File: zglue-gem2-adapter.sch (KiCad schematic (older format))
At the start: 77 parts, among them J1 543630489, J2 543630489, U1 zGlue-Jade

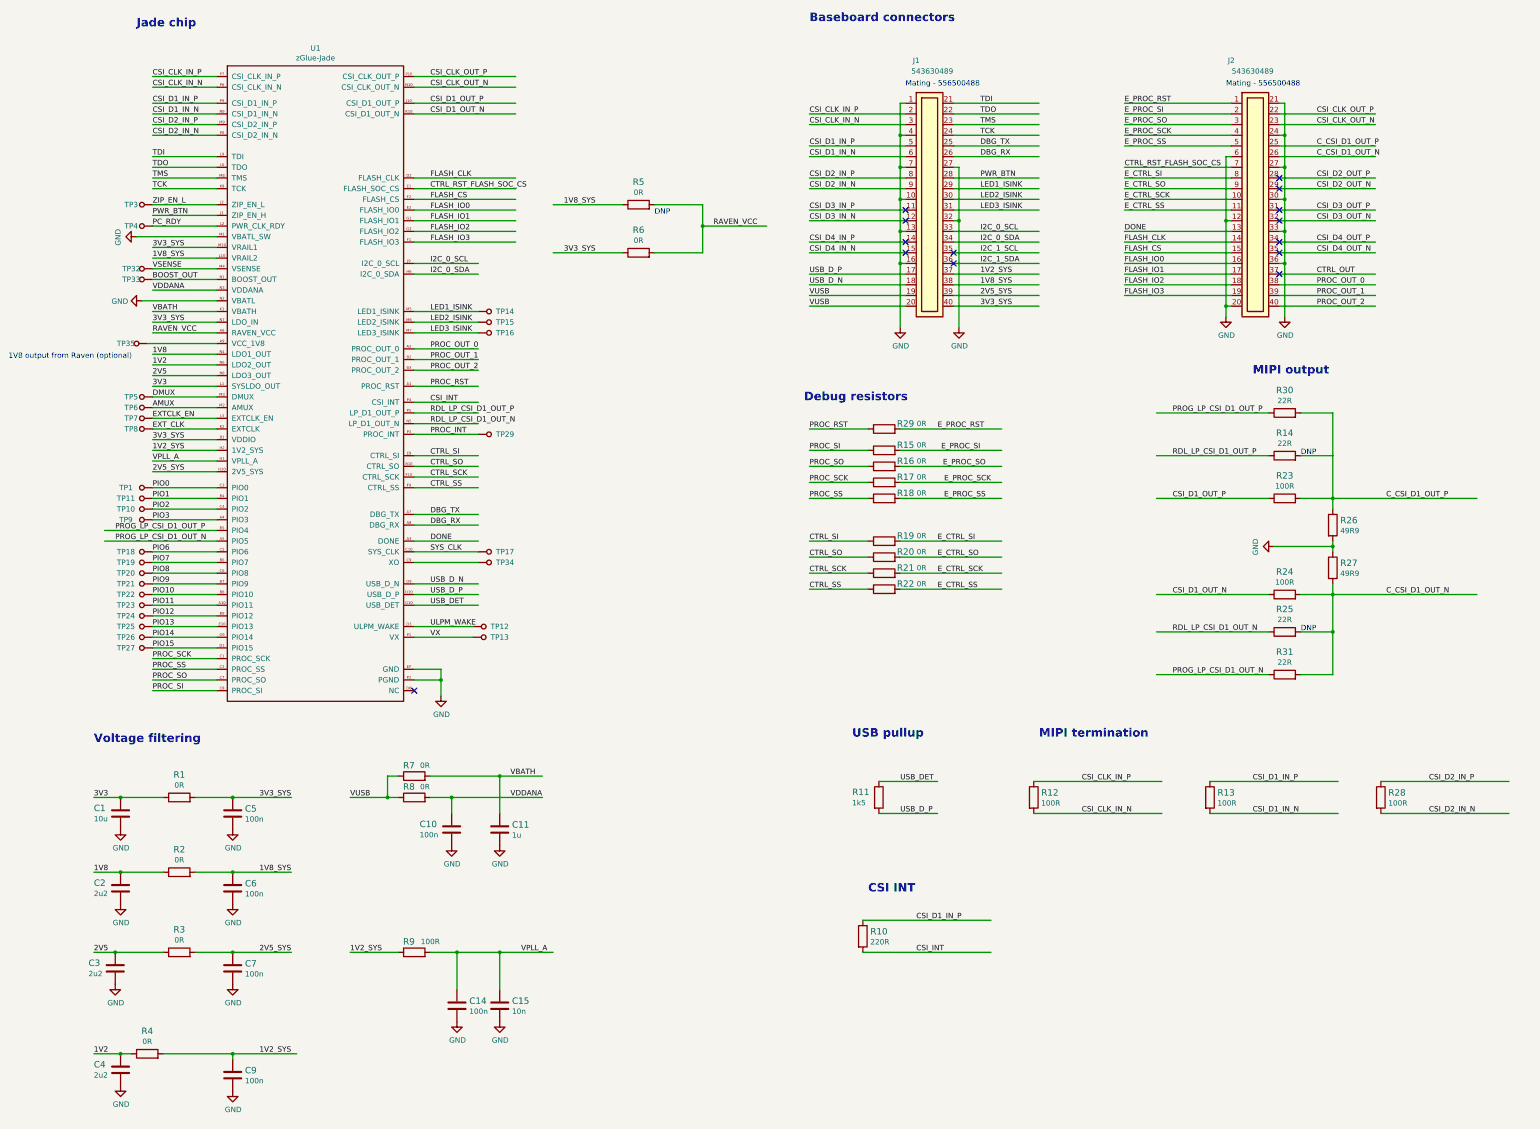
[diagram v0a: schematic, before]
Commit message: Update GEM2 symbol
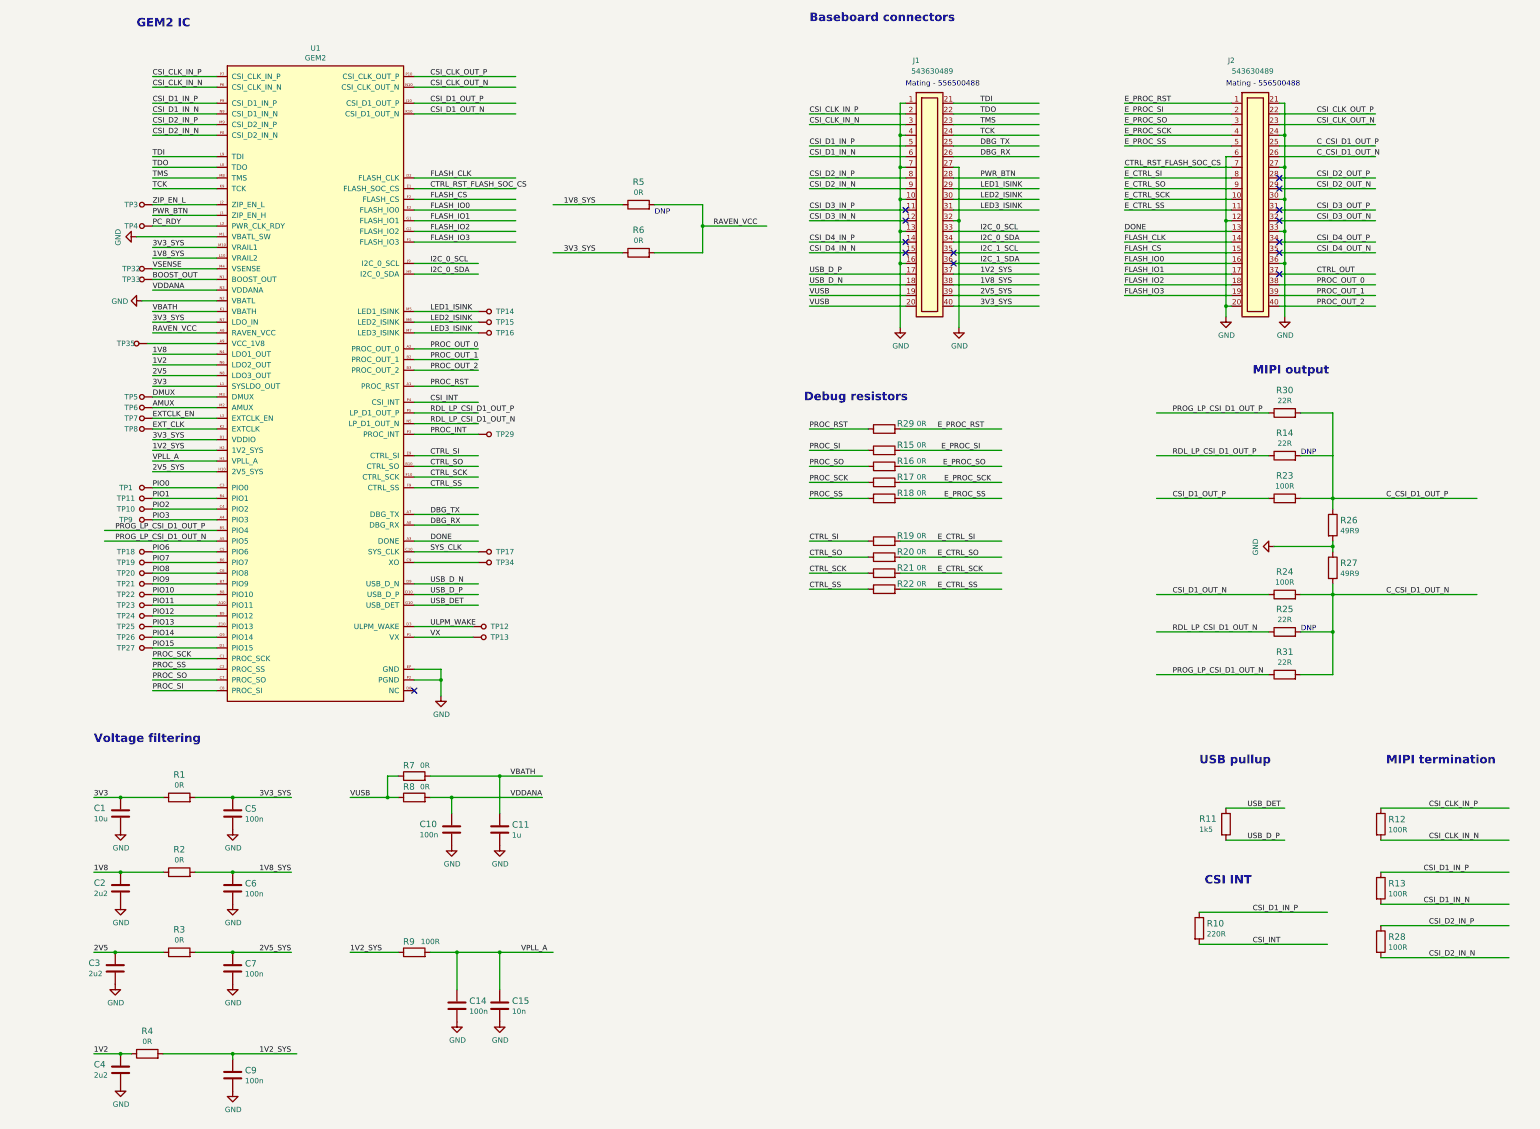
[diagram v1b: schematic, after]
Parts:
- removed U1: zGlue-Jade, zglue-jade-adapter-footprints:Z-Glue_LGA-96, symbol zglue-jade-adapter:zGlue-Jade-zglue-jade
- added U1: GEM2, zglue-jade-adapter-footprints:Z-Glue_LGA-96, symbol zglue-jade-adapter:GEM2
- R14, R25: DNP (none) -> 1
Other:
- note added: "GEM2 IC"
- note removed: "1V8 output from Raven (optional)"
- note removed: "Jade chip"
- moved on the sheet: R10, R11, R12, R13, R28
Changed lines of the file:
@@
 EESchema Schematic File Version 4
-LIBS:zglue-gem2-adapter-cache
 EELAYER 30 0
 EELAYER END
@@
 1V2
 Text Notes 1600 850  0    79   ~ 16
-Jade chip
+GEM2 IC
 $Comp
 L zglue-jade-adapter:C_100n_0402_6V3 C5
@@
 Text Label 10850 2750 0    50   ~ 0
 DONE
-Text Label 8750 7900 0    50   ~ 0
+Text Label 12000 8150 0    50   ~ 0
 USB_DET
 Text Label 7900 3250 0    50   ~ 0
@@
 L zglue-jade-adapter:R_1k5_0402 R11
 U 1 1 5DCE918C
-P 8550 8050
-F 0 "R11" V 8500 7800 60  0000 L CNN
-F 1 "R_1k5_0402" H 8550 7900 60  0001 C CNN
-F 2 "zglue-jade-adapter-footprints:0402-res" H 8750 8250 60  0001 L CNN
-F 3 "" H 8550 8050 50  0001 C CNN
-F 4 "PANASONIC_ELECTRONIC_COMPONENTS" H 8750 8450 60  0001 L CNN "Manufacturer"
-F 5 "ERJ2RKF1501X" H 8750 8350 60  0001 L CNN "MPN"
-F 6 "1k5" V 8600 7800 50  0000 L CNN "Val"
-	1    8550 8050
-	0    1    1    0
-$EndComp
-Text Label 8750 8200 0    50   ~ 0
+P 11800 8300
+F 0 "R11" V 11750 8050 60  0000 L CNN
+F 1 "R_1k5_0402" H 11800 8150 60  0001 C CNN
+F 2 "zglue-jade-adapter-footprints:0402-res" H 12000 8500 60  0001 L CNN
+F 3 "" H 11800 8300 50  0001 C CNN
+F 4 "PANASONIC_ELECTRONIC_COMPONENTS" H 12000 8700 60  0001 L CNN "Manufacturer"
+F 5 "ERJ2RKF1501X" H 12000 8600 60  0001 L CNN "MPN"
+F 6 "1k5" V 11850 8050 50  0000 L CNN "Val"
+	1    11800 8300
+	0    1    1    0
+$EndComp
+Text Label 12000 8450 0    50   ~ 0
 USB_D_P
 Wire Wire Line
-	8550 7900 9100 7900
-Wire Wire Line
-	8550 8200 9100 8200
+	11800 8150 12350 8150
+Wire Wire Line
+	11800 8450 12350 8450
 Text Notes 8800 1400 0    50   ~ 0
 Mating - 556500488
@@
 Wire Wire Line
 	8750 6100 9700 6100
-Text Notes 8300 7500 0    79   ~ 16
+Text Notes 11550 7750 0    79   ~ 16
 USB pullup
 Text Label 9500 2350 0    50   ~ 0
@@
 Wire Wire Line
 	2350 3800 1700 3800
-Text Notes 400  3950 0    50   ~ 0
-1V8 output from Raven (optional)
 Wire Wire Line
 	1850 10450 2500 10450
@@
 L zglue-jade-adapter:R_100R_0402 R12
 U 1 1 5DC3B849
-P 10000 8050
-F 0 "R12" V 9955 8120 60  0000 L CNN
-F 1 "R_100R_0402" H 10000 7900 60  0001 C CNN
-F 2 "zglue-jade-adapter-footprints:0402-res" H 10200 8250 60  0001 L CNN
-F 3 "" H 10000 8050 50  0001 C CNN
-F 4 "BOURNS" H 10200 8450 60  0001 L CNN "Manufacturer"
-F 5 "CR0402-FX-1000GLF" H 10200 8350 60  0001 L CNN "MPN"
-F 6 "100R" V 10053 8120 50  0000 L CNN "Val"
-	1    10000 8050
-	0    1    1    0
-$EndComp
-Wire Wire Line
-	10000 7900 11200 7900
-Wire Wire Line
-	10000 8200 11200 8200
-Text Label 10450 7900 0    50   ~ 0
+P 13250 8300
+F 0 "R12" V 13205 8370 60  0000 L CNN
+F 1 "R_100R_0402" H 13250 8150 60  0001 C CNN
+F 2 "zglue-jade-adapter-footprints:0402-res" H 13450 8500 60  0001 L CNN
+F 3 "" H 13250 8300 50  0001 C CNN
+F 4 "BOURNS" H 13450 8700 60  0001 L CNN "Manufacturer"
+F 5 "CR0402-FX-1000GLF" H 13450 8600 60  0001 L CNN "MPN"
+F 6 "100R" V 13303 8370 50  0000 L CNN "Val"
+	1    13250 8300
+	0    1    1    0
+$EndComp
+Wire Wire Line
+	13250 8150 14450 8150
+Wire Wire Line
+	13250 8450 14450 8450
+Text Label 13700 8150 0    50   ~ 0
 CSI_CLK_IN_P
-Text Label 10450 8200 0    50   ~ 0
+Text Label 13700 8450 0    50   ~ 0
 CSI_CLK_IN_N
 $Comp
 L zglue-jade-adapter:R_100R_0402 R13
 U 1 1 5DC8AA98
-P 11650 8050
-F 0 "R13" V 11605 8120 60  0000 L CNN
-F 1 "R_100R_0402" H 11650 7900 60  0001 C CNN
-F 2 "zglue-jade-adapter-footprints:0402-res" H 11850 8250 60  0001 L CNN
-F 3 "" H 11650 8050 50  0001 C CNN
-F 4 "BOURNS" H 11850 8450 60  0001 L CNN "Manufacturer"
-F 5 "CR0402-FX-1000GLF" H 11850 8350 60  0001 L CNN "MPN"
-F 6 "100R" V 11703 8120 50  0000 L CNN "Val"
-	1    11650 8050
-	0    1    1    0
-$EndComp
-Wire Wire Line
-	11650 7900 12850 7900
-Wire Wire Line
-	11650 8200 12850 8200
+P 13250 8900
+F 0 "R13" V 13205 8970 60  0000 L CNN
+F 1 "R_100R_0402" H 13250 8750 60  0001 C CNN
+F 2 "zglue-jade-adapter-footprints:0402-res" H 13450 9100 60  0001 L CNN
+F 3 "" H 13250 8900 50  0001 C CNN
+F 4 "BOURNS" H 13450 9300 60  0001 L CNN "Manufacturer"
+F 5 "CR0402-FX-1000GLF" H 13450 9200 60  0001 L CNN "MPN"
+F 6 "100R" V 13303 8970 50  0000 L CNN "Val"
+	1    13250 8900
+	0    1    1    0
+$EndComp
+Wire Wire Line
+	13250 8750 14450 8750
+Wire Wire Line
+	13250 9050 14450 9050
 $Comp
 L zglue-jade-adapter:R_100R_0402 R28
 U 1 1 5DCA538B
-P 13250 8050
-F 0 "R28" V 13205 8120 60  0000 L CNN
-F 1 "R_100R_0402" H 13250 7900 60  0001 C CNN
-F 2 "zglue-jade-adapter-footprints:0402-res" H 13450 8250 60  0001 L CNN
-F 3 "" H 13250 8050 50  0001 C CNN
-F 4 "BOURNS" H 13450 8450 60  0001 L CNN "Manufacturer"
-F 5 "CR0402-FX-1000GLF" H 13450 8350 60  0001 L CNN "MPN"
-F 6 "100R" V 13303 8120 50  0000 L CNN "Val"
-	1    13250 8050
-	0    1    1    0
-$EndComp
-Wire Wire Line
-	13250 7900 14450 7900
-Wire Wire Line
-	13250 8200 14450 8200
-Text Label 12050 7900 0    50   ~ 0
+P 13250 9400
+F 0 "R28" V 13205 9470 60  0000 L CNN
+F 1 "R_100R_0402" H 13250 9250 60  0001 C CNN
+F 2 "zglue-jade-adapter-footprints:0402-res" H 13450 9600 60  0001 L CNN
+F 3 "" H 13250 9400 50  0001 C CNN
+F 4 "BOURNS" H 13450 9800 60  0001 L CNN "Manufacturer"
+F 5 "CR0402-FX-1000GLF" H 13450 9700 60  0001 L CNN "MPN"
+F 6 "100R" V 13303 9470 50  0000 L CNN "Val"
+	1    13250 9400
+	0    1    1    0
+$EndComp
+Wire Wire Line
+	13250 9250 14450 9250
+Wire Wire Line
+	13250 9550 14450 9550
+Text Label 13650 8750 0    50   ~ 0
 CSI_D1_IN_P
-Text Label 12050 8200 0    50   ~ 0
+Text Label 13650 9050 0    50   ~ 0
 CSI_D1_IN_N
-Text Label 13700 7900 0    50   ~ 0
+Text Label 13700 9250 0    50   ~ 0
 CSI_D2_IN_P
-Text Label 13700 8200 0    50   ~ 0
+Text Label 13700 9550 0    50   ~ 0
 CSI_D2_IN_N
-Text Label 8900 9500 0    50   ~ 0
+Text Label 12050 9425 0    50   ~ 0
 CSI_INT
 $Comp
 L zglue-jade-adapter:R_220R_0402 R10
 U 1 1 5DCC486C
-P 8400 9350
-F 0 "R10" V 8355 9420 60  0000 L CNN
-F 1 "R_220R_0402" H 8400 9200 60  0001 C CNN
-F 2 "zglue-jade-adapter-footprints:0402-res" H 8600 9550 60  0001 L CNN
-F 3 "" H 8400 9350 50  0001 C CNN
-F 4 "TE_CONNECTIVITY_/_NEOHM" H 8600 9750 60  0001 L CNN "Manufacturer"
-F 5 "CRG0402J220R" H 8600 9650 60  0001 L CNN "MPN"
-F 6 "220R" V 8453 9420 50  0000 L CNN "Val"
-	1    8400 9350
-	0    1    1    0
-$EndComp
-Wire Wire Line
-	8400 9200 9600 9200
-Wire Wire Line
-	8400 9500 9600 9500
-Text Label 8900 9200 0    50   ~ 0
+P 11550 9275
+F 0 "R10" V 11505 9345 60  0000 L CNN
+F 1 "R_220R_0402" H 11550 9125 60  0001 C CNN
+F 2 "zglue-jade-adapter-footprints:0402-res" H 11750 9475 60  0001 L CNN
+F 3 "" H 11550 9275 50  0001 C CNN
+F 4 "TE_CONNECTIVITY_/_NEOHM" H 11750 9675 60  0001 L CNN "Manufacturer"
+F 5 "CRG0402J220R" H 11750 9575 60  0001 L CNN "MPN"
+F 6 "220R" V 11603 9345 50  0000 L CNN "Val"
+	1    11550 9275
+	0    1    1    0
+$EndComp
+Wire Wire Line
+	11550 9125 12750 9125
+Wire Wire Line
+	11550 9425 12750 9425
+Text Label 12050 9125 0    50   ~ 0
 CSI_D1_IN_P
-Text Notes 10050 7500 0    79   ~ 16
+Text Notes 13300 7750 0    79   ~ 16
 MIPI termination
-Text Notes 8450 8950 0    79   ~ 16
+Text Notes 11600 8875 0    79   ~ 16
 CSI INT
 $Comp
@@
 F 5 "CRCW040222R0FKED" H 12550 5150 60  0001 L CNN "MPN"
 F 6 "22R" H 12350 4965 50  0000 C CNN "Val"
+F 7 "1" H 12350 4850 50  0001 C CNN "DNP"
 	1    12350 4850
 	1    0    0    -1
@@
 F 5 "CRCW040222R0FKED" H 12550 6800 60  0001 L CNN "MPN"
 F 6 "22R" H 12350 6615 50  0000 C CNN "Val"
+F 7 "1" H 12350 6500 50  0001 C CNN "DNP"
 	1    12350 6500
 	1    0    0    -1
@@
 	2350 2600 1750 2600
 $Comp
-L zglue-jade-adapter:zGlue-Jade-zglue-jade U1
-U 1 1 5DB41B4F
+L zglue-jade-adapter:GEM2 U1
+U 1 1 5ED52858
 P 3200 3450
 F 0 "U1" H 3275 5865 50  0000 C CNN
-F 1 "zGlue-Jade" H 3275 5774 50  0000 C CNN
+F 1 "GEM2" H 3275 5774 50  0000 C CNN
 F 2 "zglue-jade-adapter-footprints:Z-Glue_LGA-96" H 3200 3450 50  0001 C CNN
 F 3 "" H 3200 3450 50  0001 C CNN

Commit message: Make more space on schematic sheet
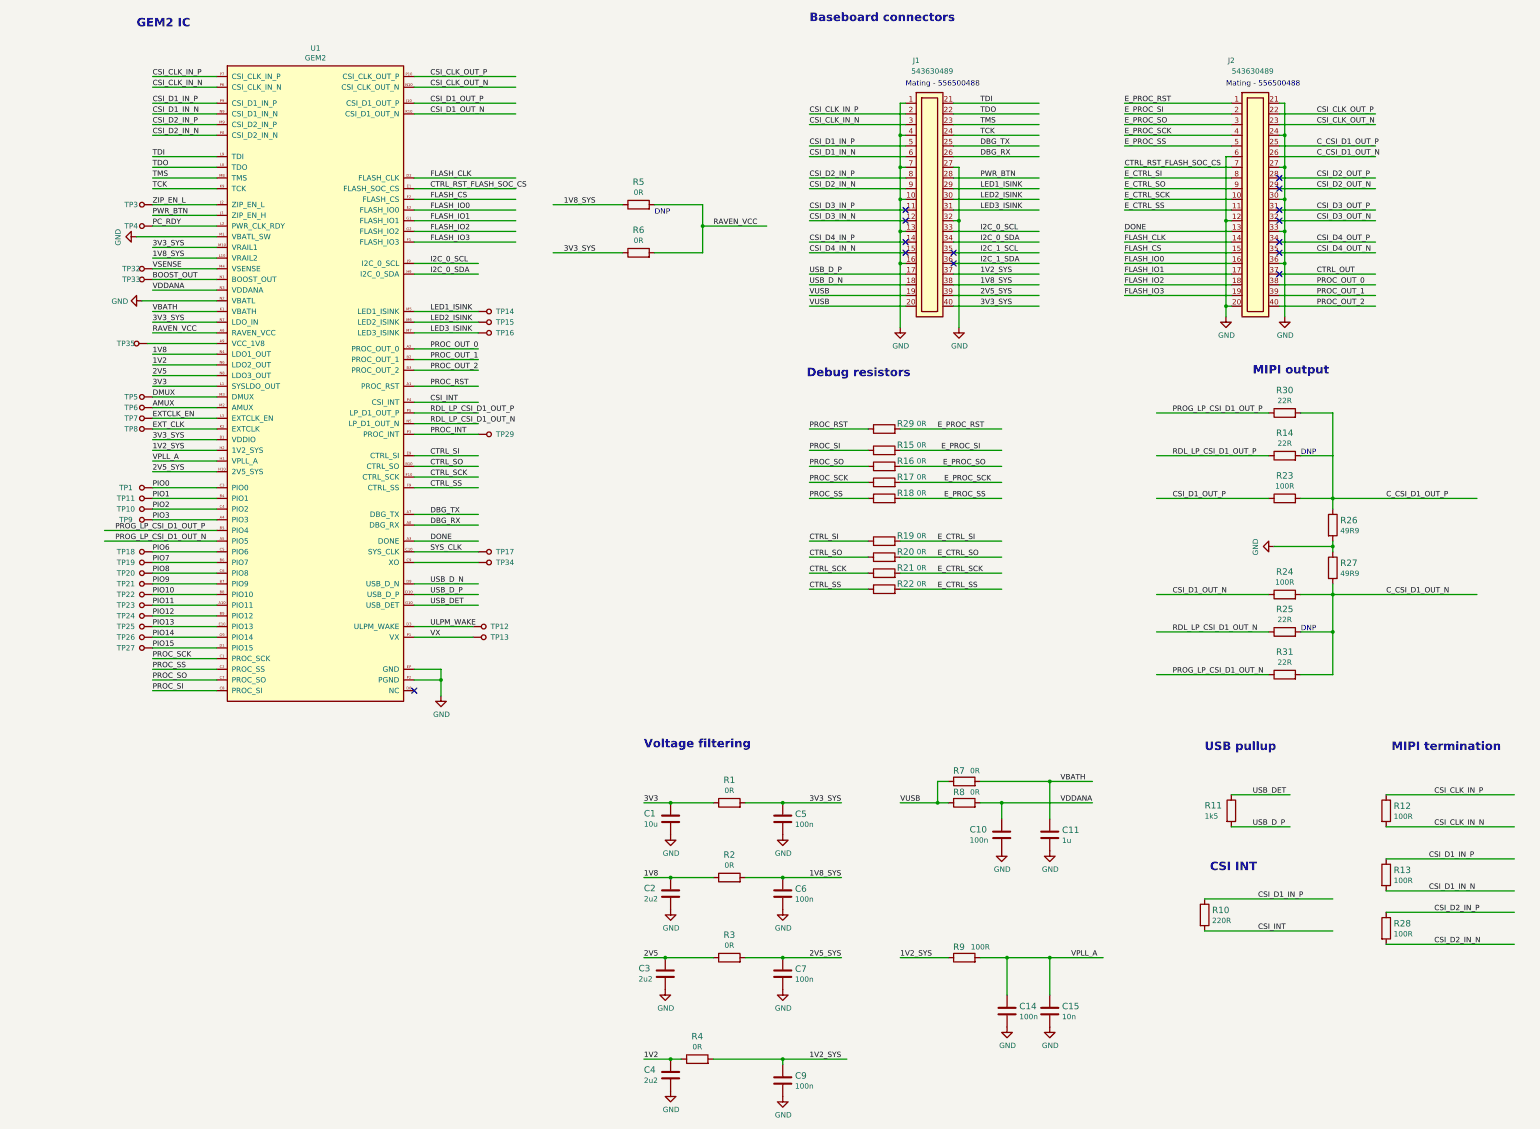
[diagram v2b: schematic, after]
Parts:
- R5: DNP (none) -> 1
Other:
- moved on the sheet: C1, C10, C11, C14, C15, C2, C3, C4, C5, C6, C7, C9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
